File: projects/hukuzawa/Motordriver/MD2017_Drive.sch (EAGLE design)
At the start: 22 parts

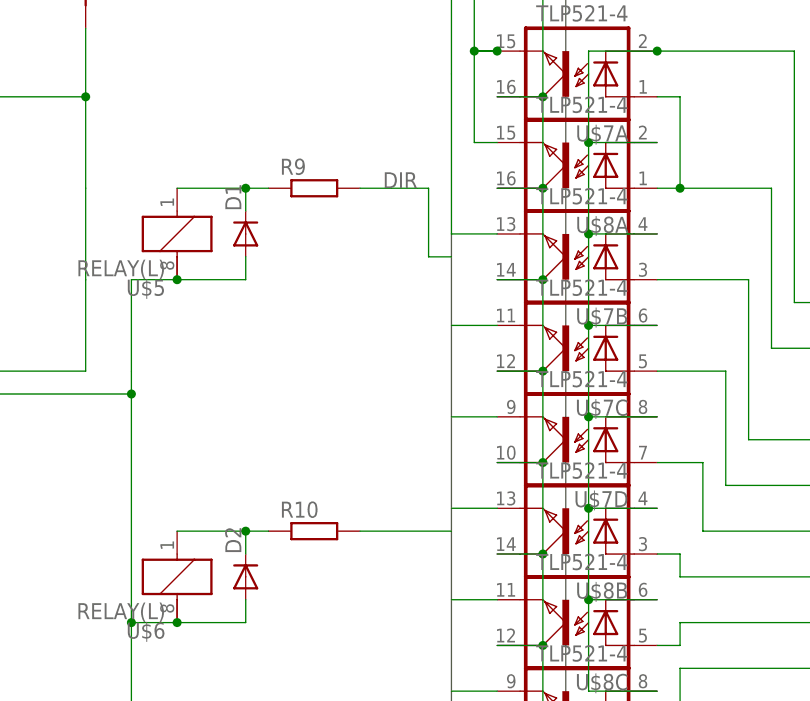
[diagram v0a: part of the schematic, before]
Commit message: モータードライバ修正
すべての配線の名前を変更
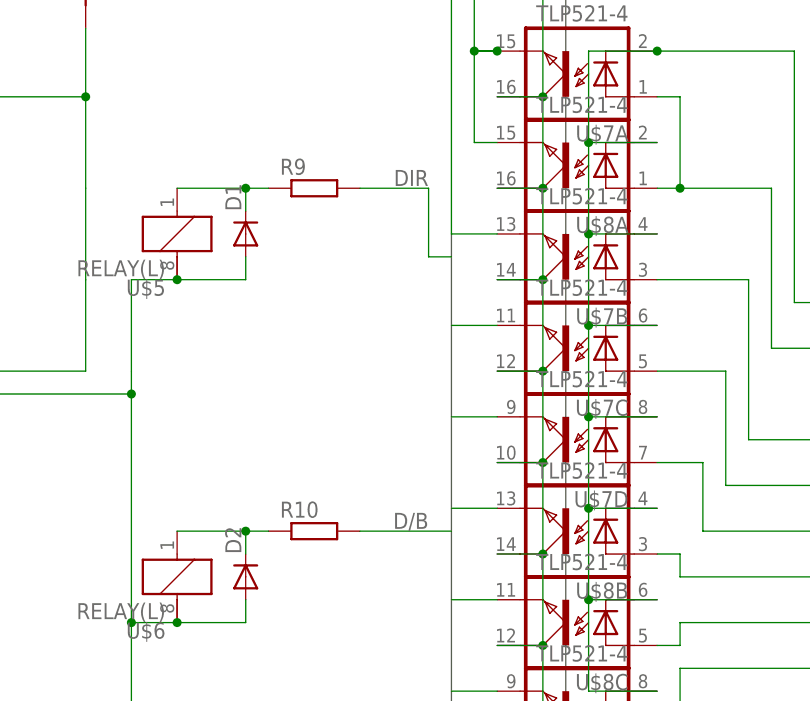
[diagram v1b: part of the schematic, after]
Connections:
- net 11 renamed NDSUPP2
- net 2 renamed NSIG6
- net 3 renamed NSIG5
- net 4 renamed NSIG4
- net 5 renamed NSIG3
- net 6 renamed NSIG2
- net 7 renamed NSIG1
- net 8 renamed NCSUPP1
- net N$9 renamed NDSUPP1
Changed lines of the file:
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@@
 </busses>
 <nets>
-<net name="8" class="0">
+<net name="NCSUPP1" class="0">
 <segment>
 <pinref part="U$7" gate="A" pin="A"/>
@@
 </segment>
 </net>
-<net name="7" class="0">
+<net name="NSIG1" class="0">
 <segment>
 <wire x1="48.26" y1="-20.32" x2="35.56" y2="-20.32" width="0.1524" layer="91"/>
@@
 </segment>
 </net>
-<net name="6" class="0">
+<net name="NSIG2" class="0">
 <segment>
 <wire x1="48.26" y1="-25.4" x2="33.02" y2="-25.4" width="0.1524" layer="91"/>
@@
 </segment>
 </net>
-<net name="5" class="0">
+<net name="NSIG3" class="0">
 <segment>
 <wire x1="48.26" y1="-30.48" x2="30.48" y2="-30.48" width="0.1524" layer="91"/>
@@
 </segment>
 </net>
-<net name="4" class="0">
+<net name="NSIG4" class="0">
 <segment>
 <wire x1="48.26" y1="-35.56" x2="27.94" y2="-35.56" width="0.1524" layer="91"/>
@@
 </segment>
 </net>
-<net name="3" class="0">
+<net name="NSIG5" class="0">
 <segment>
 <wire x1="48.26" y1="-40.64" x2="27.94" y2="-40.64" width="0.1524" layer="91"/>
@@
 </segment>
 </net>
-<net name="2" class="0">
+<net name="NSIG6" class="0">
 <segment>
 <wire x1="48.26" y1="-45.72" x2="27.94" y2="-45.72" width="0.1524" layer="91"/>
@@
 <wire x1="0" y1="0" x2="0" y2="7.62" width="0.1524" layer="91"/>
 <wire x1="0" y1="7.62" x2="-7.62" y2="7.62" width="0.1524" layer="91"/>
-<label x="-5.08" y="7.62" size="1.778" layer="95"/>
 <pinref part="R9" gate="G$1" pin="2"/>
+<label x="0" y="7.874" size="1.778" layer="95" rot="MR0"/>
 </segment>
 </net>
@@
 </segment>
 </net>
-<net name="N$9" class="0">
+<net name="NDSUPP1" class="0">
 <segment>
 <pinref part="U$5" gate="1" pin="1"/>
@@
 </segment>
 </net>
-<net name="11" class="0">
+<net name="NDSUPP2" class="0">
 <segment>
 <pinref part="U$6" gate="1" pin="1"/>
@@
 <pinref part="R10" gate="G$1" pin="2"/>
 <wire x1="-7.62" y1="-30.48" x2="2.54" y2="-30.48" width="0.1524" layer="91"/>
-</segment>
-<segment>
+<label x="0" y="-30.226" size="1.778" layer="95" rot="MR0"/>
+</segment>
+<segment>
